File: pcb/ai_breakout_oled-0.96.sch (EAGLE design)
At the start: 23 parts, among them IC1 74HCT245MTC, J1 2X04, J2 1X08, M1 STAND-OFF, M2 STAND-OFF, M3 STAND-OFF, M4 STAND-OFF, U1 UG-2864HSWEG01, U2 MIC5205-3.3

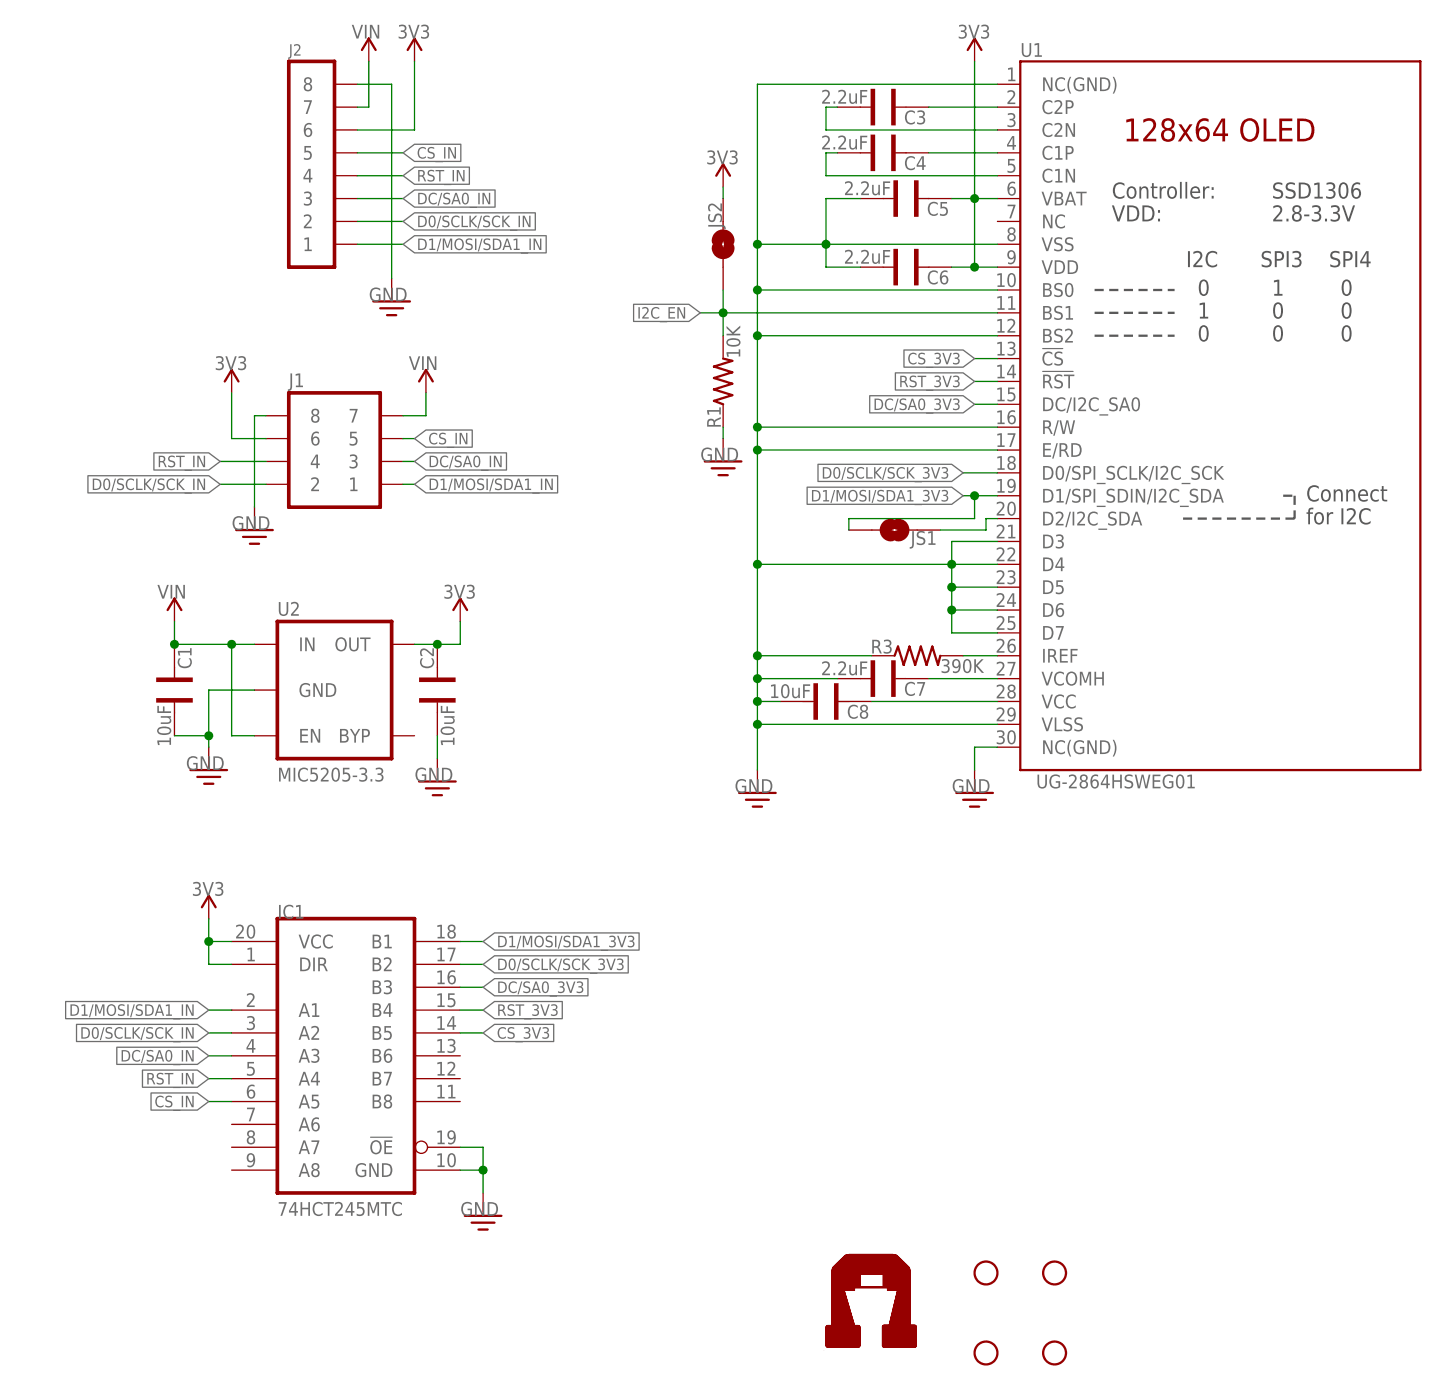
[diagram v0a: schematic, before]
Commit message: Adding BOM.  Minor silkscreen changes
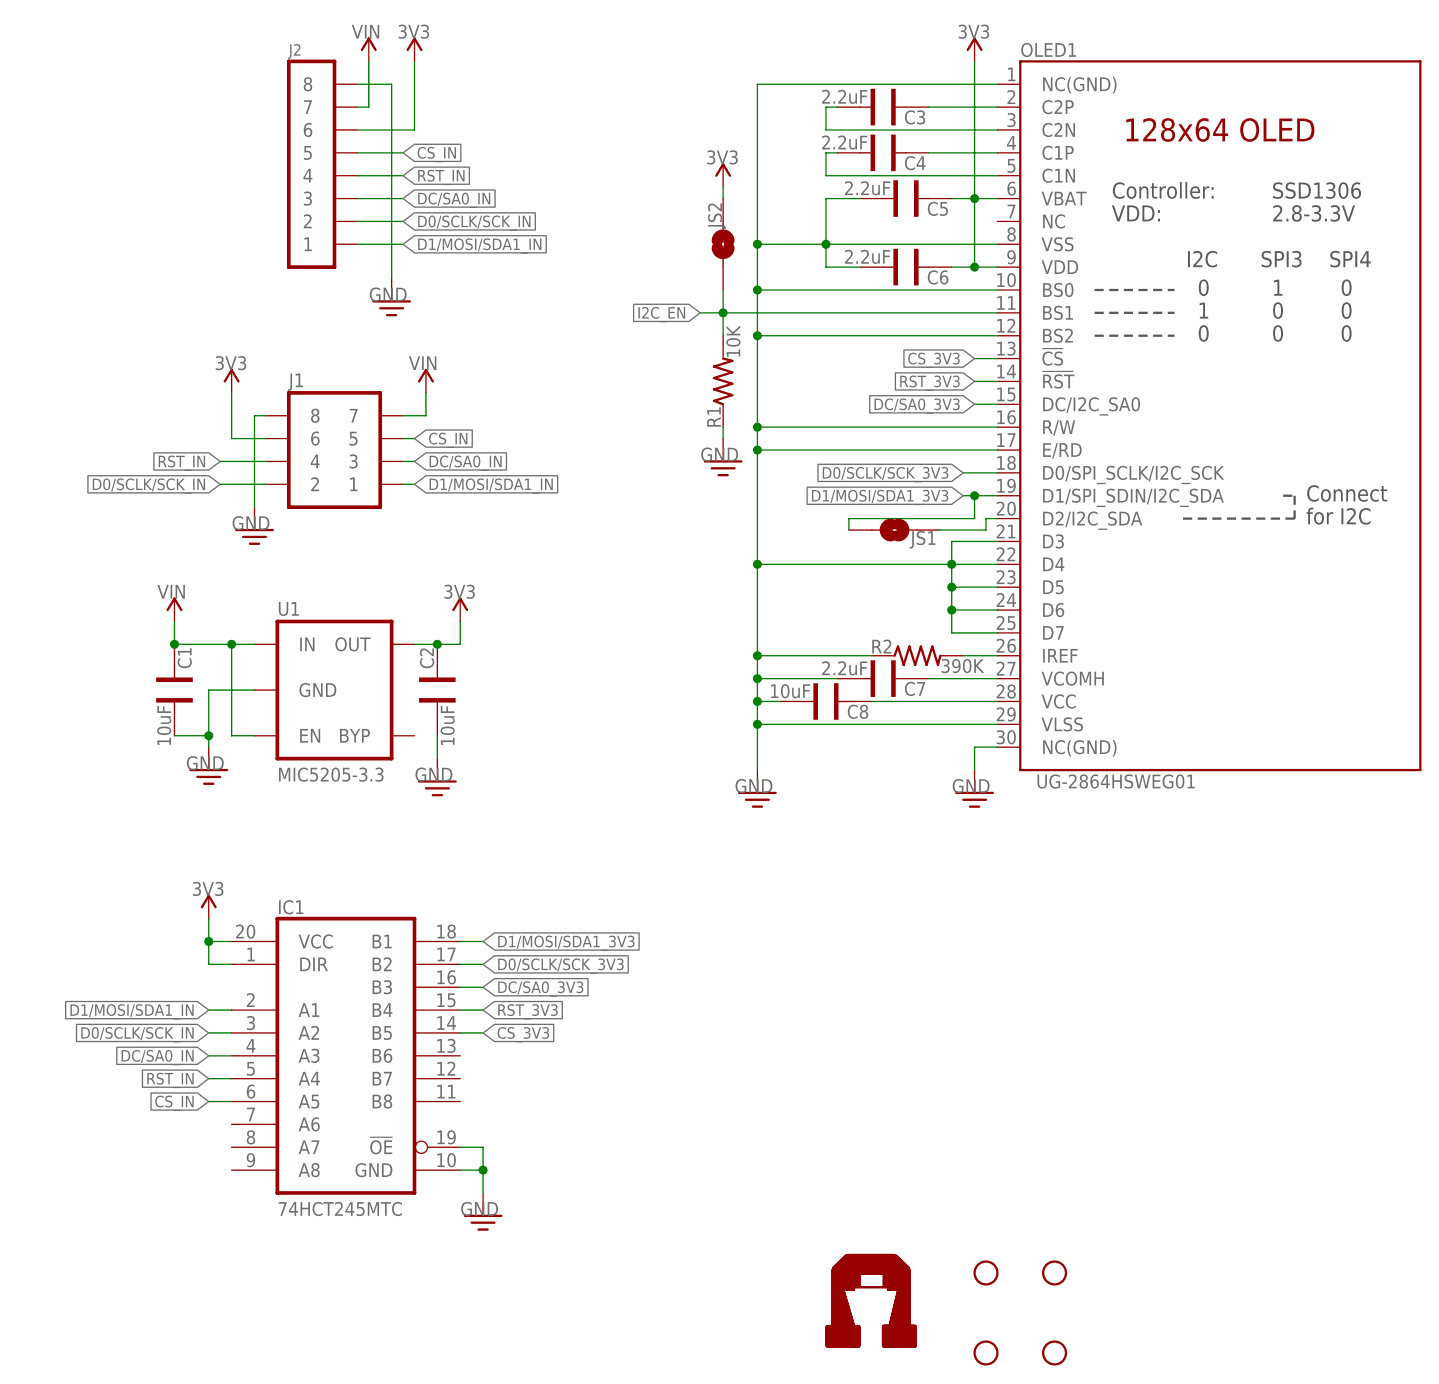
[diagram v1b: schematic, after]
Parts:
- removed U2: MIC5205-3.3, Ai_Power:MIC5205-3.3
- added OLED1: UG-2864HSWEG01, Ai_Displays:UG-2864HSWEG01-0.96
- U1: value UG-2864HSWEG01 -> MIC5205-3.3; device Ai_Displays:UG-2864HSWEG01-0.96 -> Ai_Power:MIC5205-3.3
- renumbered R3 to R2
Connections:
- net 3V3: now also OLED1.VBAT, OLED1.VDD, U1.OUT; no longer U1.VBAT, U1.VDD, U2.OUT
- net CS_3V3: now also OLED1.!CS; no longer U1.!CS
- net D0/SCLK/SCK_3V3: now also OLED1.D0/SPI_SCLK/I2C_SCK; no longer U1.D0/SPI_SCLK/I2C_SCK
- net D1/MOSI/SDA1_3V3: now also OLED1.D1/SPI_SDIN/I2C_SDA; no longer U1.D1/SPI_SDIN/I2C_SDA
- net DC/SA0_3V3: now also OLED1.DC/I2C_SA0; no longer U1.DC/I2C_SA0
- net GND: now also OLED1.BS0, OLED1.BS2, OLED1.D3, OLED1.D4, OLED1.D5, OLED1.D6, OLED1.D7, OLED1.E/RD, OLED1.NC(GND)@1, OLED1.NC(GND)@2, OLED1.R/W, OLED1.VLSS, OLED1.VSS, U1.GND; no longer U1.BS0, U1.BS2, U1.D3, U1.D4, U1.D5, U1.D6, U1.D7, U1.E/RD, U1.NC(GND)@1, U1.NC(GND)@2, U1.R/W, U1.VLSS, U1.VSS, U2.GND
- net I2C_EN: now also OLED1.BS1; no longer U1.BS1
- net N$11: now also OLED1.VCC; no longer U1.VCC
- net N$12: now also OLED1.VCOMH; no longer U1.VCOMH
- net N$3: now also OLED1.IREF; no longer U1.IREF
- net N$4: now also OLED1.C2P; no longer U1.C2P
- net N$5: now also OLED1.C2N; no longer U1.C2N
- net N$6: now also OLED1.C1P; no longer U1.C1P
- net N$7: now also OLED1.C1N; no longer U1.C1N
- net N$8: now also OLED1.D2/I2C_SDA; no longer U1.D2/I2C_SDA
- net RST_3V3: now also OLED1.!RST; no longer U1.!RST
- net VIN: now also U1.EN, U1.IN; no longer U2.EN, U2.IN
